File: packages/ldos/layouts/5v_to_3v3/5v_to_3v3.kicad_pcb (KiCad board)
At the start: 2 copper layers, 3 parts, among them U1 LDO Vin max Iq

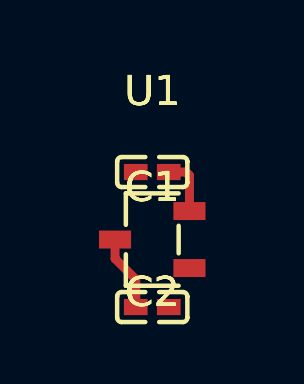
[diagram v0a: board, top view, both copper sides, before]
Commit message: Build all packages without designators on silkscreen.
Also disable fail_on_drc and enable keep_picked_parts for build
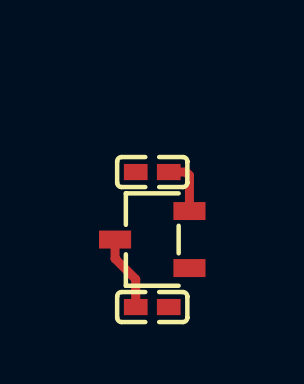
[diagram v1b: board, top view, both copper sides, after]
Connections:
- C1 pad 1: hv-1 -> hv
- C2 pad 1: hv -> hv-1
- U1 pad 2: hv -> hv-1
- U1 pad 3: hv-1 -> hv
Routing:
- net hv-1: track 2.54 -> 1.92 mm
- net hv: track 1.92 -> 2.54 mm

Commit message: [Publish] Rebuild modules (with no dep on upstream atopile pr) (#5)
* Fixes image link on published packages
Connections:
- C1 pad 1: hv -> hv-1
- C2 pad 1: hv-1 -> hv
- U1 pad 2: hv-1 -> hv
- U1 pad 3: hv -> hv-1
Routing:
- net hv-1: track 1.92 -> 2.54 mm
- net hv: track 2.54 -> 1.92 mm
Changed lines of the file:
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@@
     (net 0 "")
     (net 1 "gnd")
-    (net 2 "hv-1")
-    (net 3 "hv")
+    (net 2 "hv")
+    (net 3 "hv-1")
     (footprint "atopile:SOT-23-3_L2.9-W1.6-P1.90-LS2.8-BR-186170"
         (layer "F.Cu")
@@
             (size 1.07 0.6)
             (layers "F.Cu" "F.Mask" "F.Paste")
-            (net 2 "hv-1")
+            (net 2 "hv")
         )
         (pad "3" smd rect
@@
             (size 1.07 0.6)
             (layers "F.Cu" "F.Mask" "F.Paste")
-            (net 3 "hv")
+            (net 3 "hv-1")
         )
         (embedded_fonts no)
@@
             (size 0.79 0.54)
             (layers "F.Cu" "F.Mask" "F.Paste")
-            (net 2 "hv-1")
+            (net 2 "hv")
         )
         (pad "2" smd rect
@@
             (size 0.79 0.54)
             (layers "F.Cu" "F.Mask" "F.Paste")
-            (net 3 "hv")
+            (net 3 "hv-1")
         )
         (pad "2" smd rect

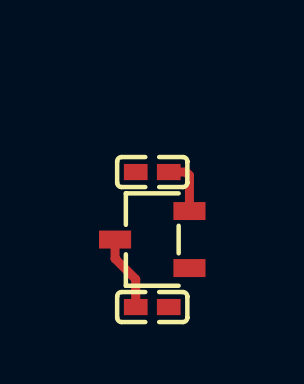
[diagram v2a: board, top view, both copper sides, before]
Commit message: Add various new packages (#14)
Add:
- DCDC converters
- Connectors

Update:
- logic
  - add dual buffer
- ldos
  - change to better default ldo
- usb
  - add missing connection
- switches
  - update rotary encoder advanced layout
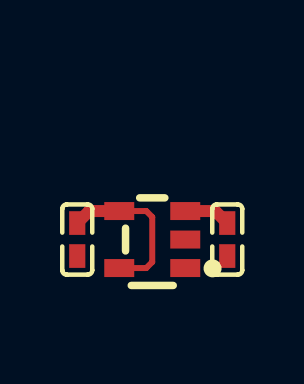
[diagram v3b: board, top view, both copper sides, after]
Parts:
- U1: value LDO Vin max Iq -> LDO 3.3V ±0% 850.5mA 320mV Vin max 3.35V Iq 10µA; footprint atopile:SOT-23-3_L2.9-W1.6-P1.90-LS2.8-BR-186170 -> atopile:SOT-23-5_L2.9-W1.6-P0.95-LS2.8-BR-2dcca4
- moved C1 3.36 mm to (-2.50, 0.00), turned to -90 degrees
- moved C2 3.36 mm to (2.50, 0.00), turned to -90 degrees
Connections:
- U1 pad 1: gnd -> hv-1
- U1 pad 2: hv -> gnd
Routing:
- net (no net): track 0.00 -> 7.00 mm
- net hv-1: track 2.54 -> 0.00 mm
- net hv: track 1.92 -> 0.00 mm

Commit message: Update packages:
- requited
- package > driver method
- cleaning up
- aligning packages
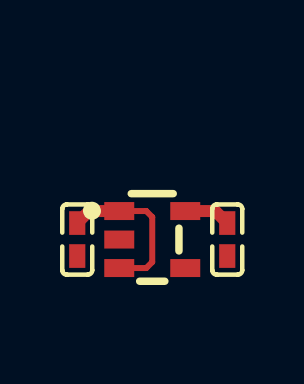
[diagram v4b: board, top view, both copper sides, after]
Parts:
- turned U1 to 180 degrees
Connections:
- C1 pad 1: hv-1 -> hv
- C2 pad 1: hv -> hv-1
- U1 pad 1: hv-1 -> hv
- U1 pad 3: hv-1 -> hv
- U1 pad 5: hv -> hv-1
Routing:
- net (no net): track 7.00 -> 0.00 mm
- net hv: track 0.00 -> 5.43 mm
- net hv-1: track 0.00 -> 1.57 mm
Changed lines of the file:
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@@
     )
     (net 0 "")
-    (net 5 "gnd")
-    (net 6 "net")
-    (net 7 "hv-1")
-    (net 8 "hv")
+    (net 1 "gnd")
+    (net 2 "net")
+    (net 3 "hv")
+    (net 4 "hv-1")
     (footprint "atopile:C0402-b3ef17"
         (layer "F.Cu")
@@
             (size 0.79 0.54)
             (layers "F.Cu" "F.Mask" "F.Paste")
-            (net 8 "hv")
+            (net 4 "hv-1")
         )
         (pad "2" smd rect
@@
             (size 0.79 0.54)
             (layers "F.Cu" "F.Mask" "F.Paste")
-            (net 5 "gnd")
+            (net 1 "gnd")
         )
         (embedded_fonts no)
@@
             (size 0.79 0.54)
             (layers "F.Cu" "F.Mask" "F.Paste")
-            (net 7 "hv-1")
+            (net 3 "hv")
         )
         (pad "2" smd rect
@@
             (size 0.79 0.54)
             (layers "F.Cu" "F.Mask" "F.Paste")
-            (net 5 "gnd")
+            (net 1 "gnd")
         )
         (embedded_fonts no)
@@
     (footprint "atopile:SOT-23-5_L2.9-W1.6-P0.95-LS2.8-BR-2dcca4"
         (layer "F.Cu")
-        (at 0 0 0)
+        (at 0 0 180)
         (property "Reference" "U1"
             (at 0 -4.95 0)
@@
                     (thickness 0.15)
                 )
-                (hide yes)
             )
         )
@@
             )
         )
+        (property "Datasheet" "https://www.lcsc.com/datasheet/lcsc_datasheet_2205241716_TECH-PUBLIC-TPAP2112K-3-3TRG1_C3021085.pdf"
+            (at 0 0 0)
+            (layer "User.9")
+            (hide yes)
+            (effects
+                (font
+                    (size 0.125 0.125)
+                    (thickness 0.01875)
+                )
+            )
+        )
+        (property "Description" ""
+            (at 0 0 0)
+            (layer "F.Fab")
+            (hide yes)
+            (effects
+                (font
+                    (size 1.27 1.27)
+                    (thickness 0.15)
+                )
+            )
+        )
         (property "__atopile_lib_fp_hash__" "ea93a946-0d80-8518-a62d-650a4778bfd6"
             (at 0 0 0)
@@
             )
         )
-        (property "Datasheet" "https://www.lcsc.com/datasheet/lcsc_datasheet_2205241716_TECH-PUBLIC-TPAP2112K-3-3TRG1_C3021085.pdf"
-            (at 0 0 0)
-            (layer "User.9")
-            (hide yes)
-            (effects
-                (font
-                    (size 0.125 0.125)
-                    (thickness 0.01875)
-                )
-            )
-        )
         (property "atopile_address" "ldo"
             (at 0 0 0)
@@
         )
         (attr smd)
+        (fp_line
+            (start -0.42 -1.39)
+            (end 0.42 -1.39)
+            (stroke
+                (width 0.25)
+                (type solid)
+            )
+            (layer "F.SilkS")
+        )
         (fp_line
             (start -0.7 1.53)
@@
         )
         (fp_line
-            (start -0.42 -1.39)
-            (end 0.42 -1.39)
-            (stroke
-                (width 0.25)
-                (type solid)
-            )
-            (layer "F.SilkS")
-        )
-        (fp_line
             (start -0.89 0.38)
             (end -0.89 -0.38)
@@
             )
             (layer "F.SilkS")
+        )
+        (fp_circle
+            (center 2.01 0.96)
+            (end 2.16 0.96)
+            (stroke
+                (width 0.3)
+                (type solid)
+            )
+            (fill no)
+            (layer "F.SilkS")
+        )
+        (fp_circle
+            (center 1.11 1.25)
+            (end 1.26 1.25)
+            (stroke
+                (width 0.3)
+                (type solid)
+            )
+            (fill no)
+            (layer "Cmts.User")
         )
         (fp_circle
@@
             (layer "F.Fab")
         )
-        (fp_circle
-            (center 1.11 1.25)
-            (end 1.26 1.25)
-            (stroke
-                (width 0.3)
-                (type solid)
-            )
-            (fill no)
-            (layer "Cmts.User")
-        )
-        (fp_circle
-            (center 2.01 0.96)
-            (end 2.16 0.96)
-            (stroke
-                (width 0.3)
-                (type solid)
-            )
-            (fill no)
-            (layer "F.SilkS")
-        )
-        (fp_text user "%R"
+        (fp_text user "${REFERENCE}"
             (at 0 0 0)
             (layer "F.Fab")
@@
                     (thickness 0.15)
                 )
+                (hide yes)
             )
             (unlocked no)
         )
-        (fp_text user "${REFERENCE}"
-            (at 0 -4.95 0)
-            (layer "F.SilkS")
-            (effects
-                (font
-                    (size 1 1)
-                    (thickness 0.15)
-                )
-                (hide yes)
-            )
-            (unlocked no)
+        (pad "1" smd rect
+            (at 1.1 0.95 270)
+            (size 0.6 1)
+            (layers "F.Cu" "F.Mask" "F.Paste")
+            (net 3 "hv")
         )
         (pad "2" smd rect
-            (at 1.1 0 90)
+            (at 1.1 0 270)
             (size 0.6 1)
-            (layers "F.Cu" "F.Paste" "F.Mask")
-            (net 5 "gnd")
+            (layers "F.Cu" "F.Mask" "F.Paste")
+            (net 1 "gnd")
         )
         (pad "3" smd rect
-            (at 1.1 -0.95 90)
+            (at 1.1 -0.95 270)
             (size 0.6 1)
-            (layers "F.Cu" "F.Paste" "F.Mask")
-            (net 7 "hv-1")
-        )
-        (pad "1" smd rect
-            (at 1.1 0.95 90)
+            (layers "F.Cu" "F.Mask" "F.Paste")
+            (net 3 "hv")
+        )
+        (pad "4" smd rect
+            (at -1.1 -0.95 270)
             (size 0.6 1)
-            (layers "F.Cu" "F.Paste" "F.Mask")
-            (net 7 "hv-1")
-        )
-        (pad "4" smd rect
-            (at -1.1 -0.95 90)
+            (layers "F.Cu" "F.Mask" "F.Paste")
+            (net 2 "net")
+        )
+        (pad "5" smd rect
+            (at -1.1 0.95 270)
             (size 0.6 1)
-            (layers "F.Cu" "F.Paste" "F.Mask")
-            (net 6 "net")
-        )
-        (pad "5" smd rect
-            (at -1.1 0.95 90)
-            (size 0.6 1)
-            (layers "F.Cu" "F.Paste" "F.Mask")
-            (net 8 "hv")
-        )
+            (layers "F.Cu" "F.Mask" "F.Paste")
+            (net 4 "hv-1")
+        )
+        (embedded_fonts no)
     )
     (embedded_fonts no)
@@
         (end -1.1 -0.95)
         (width 0.2)
-        (net 0)
+        (net 3)
+        (layer "F.Cu")
+    )
+    (segment
+        (start -1.1 0.95)
+        (end -0.2 0.95)
+        (width 0.2)
+        (net 3)
+        (layer "F.Cu")
+    )
+    (segment
+        (start -2.5 -0.55)
+        (end -2.1 -0.95)
+        (width 0.4)
+        (net 3)
+        (layer "F.Cu")
+    )
+    (segment
+        (start 0 0.75)
+        (end 0 -0.75)
+        (width 0.2)
+        (net 3)
+        (layer "F.Cu")
+    )
+    (segment
+        (start -0.2 0.95)
+        (end 0 0.75)
+        (width 0.2)
+        (net 3)
+        (layer "F.Cu")
+    )
+    (segment
+        (start -2.1 -0.95)
+        (end -1.1 -0.95)
+        (width 0.4)
+        (net 3)
+        (layer "F.Cu")
+    )
+    (segment
+        (start 0 -0.75)
+        (end -0.2 -0.95)
+        (width 0.2)
+        (net 3)
         (layer "F.Cu")
     )
@@
         (end 2.1 -0.95)
         (width 0.4)
-        (net 0)
-        (layer "F.Cu")
-    )
-    (segment
-        (start -1.1 0.95)
-        (end -0.2 0.95)
-        (width 0.2)
-        (net 0)
+        (net 4)
         (layer "F.Cu")
     )
@@
         (end 2.5 -0.55)
         (width 0.4)
-        (net 0)
-        (layer "F.Cu")
-    )
-    (segment
-        (start -2.5 -0.55)
-        (end -2.1 -0.95)
-        (width 0.4)
-        (net 0)
-        (layer "F.Cu")
-    )
-    (segment
-        (start 0 0.75)
-        (end 0 -0.75)
-        (width 0.2)
-        (net 0)
-        (layer "F.Cu")
-    )
-    (segment
-        (start -0.2 0.95)
-        (end 0 0.75)
-        (width 0.2)
-        (net 0)
-        (layer "F.Cu")
-    )
-    (segment
-        (start -2.1 -0.95)
-        (end -1.1 -0.95)
-        (width 0.4)
-        (net 0)
-        (layer "F.Cu")
-    )
-    (segment
-        (start 0 -0.75)
-        (end -0.2 -0.95)
-        (width 0.2)
-        (net 0)
-        (layer "F.Cu")
-    )
+        (net 4)
+        (layer "F.Cu")
+    )

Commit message: Update packages to ato v0.9.x (#36)
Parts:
- C1, C2: footprint atopile:C0402-b3ef17 -> Samsung_Electro_Mechanics_CL05B104KO5NNNC:C0402
- U1: value LDO 3.3V ±0% 850.5mA 320mV Vin max 3.35V Iq 10µA -> (none); footprint atopile:SOT-23-5_L2.9-W1.6-P0.95-LS2.8-BR-2dcca4 -> TECH_PUBLIC_TPAP2112K_3_3TRG1:SOT-23-5_L2.9-W1.6-P0.95-LS2.8-BR
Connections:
- net hv-1 renamed VOUT
